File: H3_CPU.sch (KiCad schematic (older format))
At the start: 0 parts

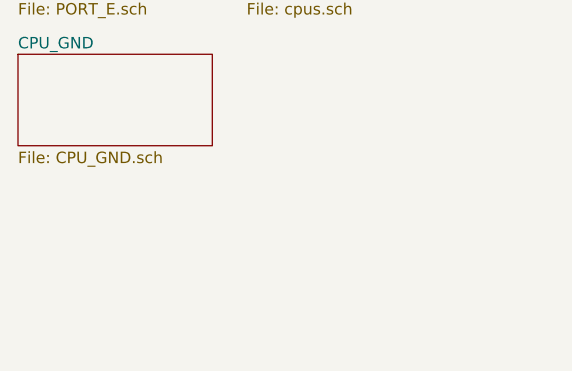
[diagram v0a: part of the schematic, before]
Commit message: update port decouple cap,
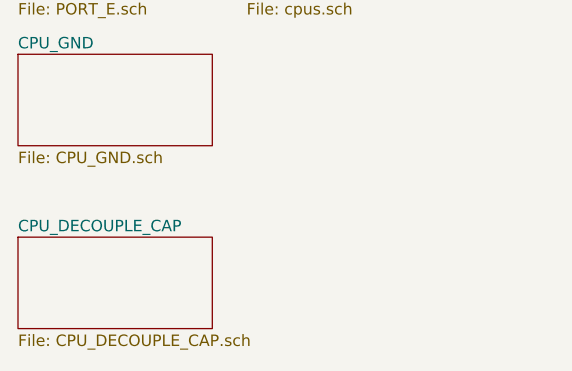
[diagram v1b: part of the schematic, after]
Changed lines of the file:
@@
 $Descr A3 16535 11693
 encoding utf-8
-Sheet 15 32
+Sheet 15 33
 Title ""
 Date ""
@@
 F1 "CPU_GND.sch" 50
 $EndSheet
+$Sheet
+S 1100 4000 850  400
+U 5C7AC496
+F0 "CPU_DECOUPLE_CAP" 50
+F1 "CPU_DECOUPLE_CAP.sch" 50
+$EndSheet
 $EndSCHEMATC
